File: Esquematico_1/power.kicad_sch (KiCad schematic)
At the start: 23 parts, among them IC1 AP2112K-3.3TRG1, U6 TPS54302DDCR

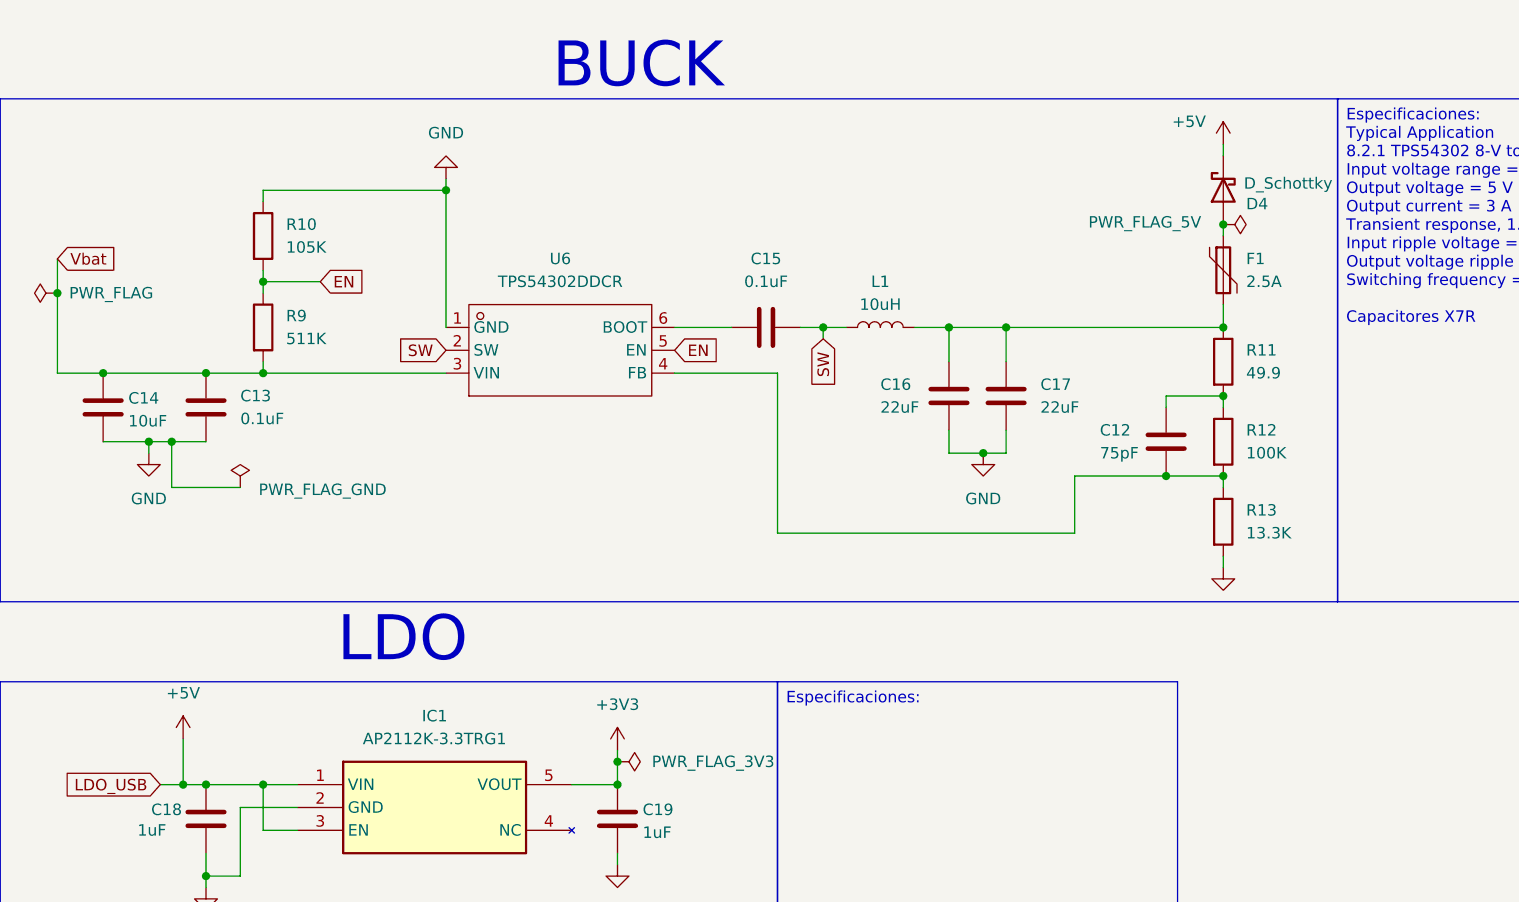
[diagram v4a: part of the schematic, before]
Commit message: Cambios netclasses, rules en el PCB, conección de los cristales
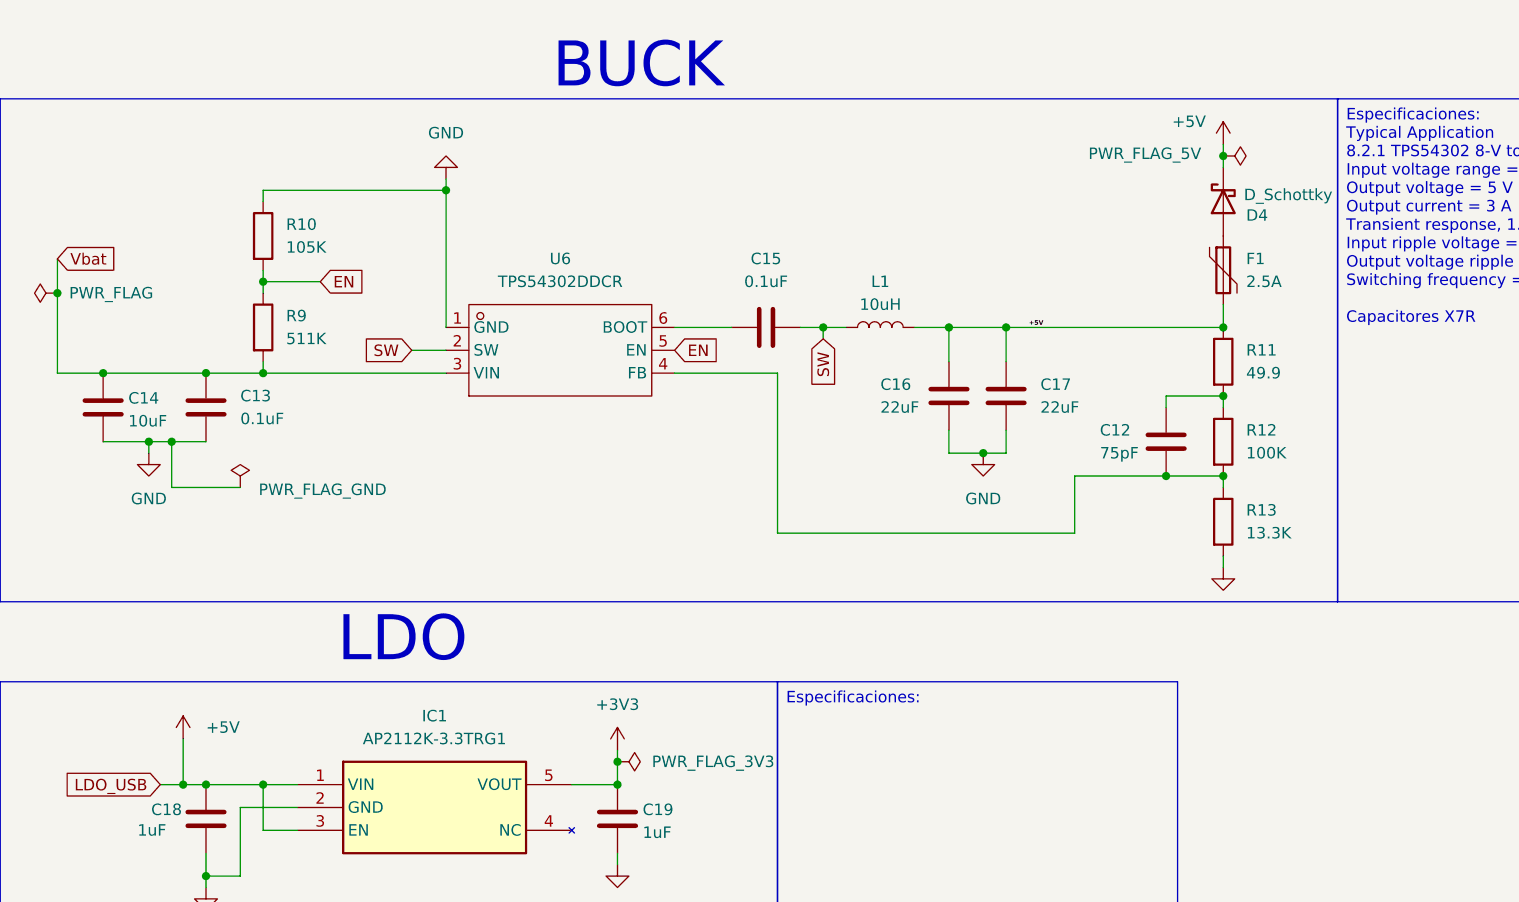
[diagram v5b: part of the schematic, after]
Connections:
- net +5V: now also C16.2, C17.2, F1.2, L1.2, R11.1
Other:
- moved on the sheet: D4
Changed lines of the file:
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@@
 	)
 	(junction
-		(at 158.75 35.56)
-		(diameter 0)
-		(color 0 0 0 0)
-	)
-	(junction
 		(at 52.07 52.07)
 		(diameter 0)
@@
 	)
 	(junction
+		(at 158.75 27.94)
+		(diameter 0)
+		(color 0 0 0 0)
+	)
+	(junction
 		(at 52.07 41.91)
 		(diameter 0)
@@
 	(wire
 		(pts
-			(xy 158.75 35.56) (xy 158.75 36.83)
-		)
-		(stroke
-			(width 0)
-			(type default)
-		)
-	)
-	(wire
-		(pts
 			(xy 114.3 46.99) (xy 111.76 46.99)
 		)
@@
 	(wire
 		(pts
+			(xy 68.58 49.53) (xy 72.39 49.53)
+		)
+		(stroke
+			(width 0)
+			(type default)
+		)
+	)
+	(wire
+		(pts
 			(xy 134.62 46.99) (xy 158.75 46.99)
 		)
@@
 	(wire
 		(pts
+			(xy 158.75 27.94) (xy 158.75 29.21)
+		)
+		(stroke
+			(width 0)
+			(type default)
+		)
+	)
+	(wire
+		(pts
 			(xy 49.53 100.33) (xy 49.53 107.95)
 		)
@@
 		)
 	)
+	(label "+5V"
+		(at 137.16 46.99 0)
+		(effects
+			(font
+				(size 0.508 0.508)
+				(thickness 0.254)
+				(bold yes)
+			)
+			(justify left bottom)
+		)
+	)
 	(global_label "Vbat"
 		(shape input)
@@
 	(global_label "SW"
 		(shape input)
-		(at 72.39 49.53 180)
+		(at 68.58 49.53 180)
 		(fields_autoplaced yes)
 		(effects
@@
 		)
 		(property "Intersheetrefs" "${INTERSHEET_REFS}"
-			(at 66.7439 49.53 0)
+			(at 62.9339 49.53 0)
 			(effects
 				(font
@@
 	(symbol
 		(lib_id "Device:D_Schottky")
-		(at 158.75 31.75 90)
+		(at 158.75 33.02 90)
 		(mirror x)
 		(unit 1)
@@
 		(dnp no)
 		(property "Reference" "D4"
-			(at 161.29 33.274 90)
+			(at 161.29 34.544 90)
 			(effects
 				(font
@@
 		)
 		(property "Value" "D_Schottky"
-			(at 161.036 30.988 90)
+			(at 161.036 32.258 90)
 			(effects
 				(font
@@
 		)
 		(property "Footprint" "Package_TO_SOT_SMD:SOT-23"
-			(at 158.75 31.75 0)
+			(at 158.75 33.02 0)
 			(effects
 				(font
@@
 		)
 		(property "Datasheet" "~"
-			(at 158.75 31.75 0)
+			(at 158.75 33.02 0)
 			(effects
 				(font
@@
 		)
 		(property "Description" "Schottky diode"
-			(at 158.75 31.75 0)
+			(at 158.75 33.02 0)
 			(effects
 				(font
@@
 	(symbol
 		(lib_id "power:PWR_FLAG")
-		(at 158.75 35.56 270)
+		(at 158.75 27.94 270)
 		(unit 1)
 		(exclude_from_sim no)
@@
 		(dnp no)
 		(property "Reference" "#FLG03"
-			(at 160.655 35.56 0)
+			(at 160.655 27.94 0)
 			(effects
 				(font
@@
 		)
 		(property "Value" "PWR_FLAG_5V"
-			(at 143.764 35.306 90)
+			(at 143.764 27.686 90)
 			(effects
 				(font
@@
 		)
 		(property "Footprint" ""
-			(at 158.75 35.56 0)
+			(at 158.75 27.94 0)
 			(effects
 				(font
@@
 		)
 		(property "Datasheet" "~"
-			(at 158.75 35.56 0)
+			(at 158.75 27.94 0)
 			(effects
 				(font
@@
 		)
 		(property "Description" "Special symbol for telling ERC where power comes from"
-			(at 158.75 35.56 0)
+			(at 158.75 27.94 0)
 			(effects
 				(font
@@
 		)
 		(instances
-			(project ""
+			(project "Esquematico_1"
 				(path "/de2d80c1-c21c-478d-b724-17659b714c38/46661298-47a8-4fc3-89be-a6732b8d105c"
 					(reference "#FLG03")
@@
 		)
 		(property "Value" "+5V"
-			(at 43.18 87.63 0)
+			(at 45.72 91.4399 0)
 			(effects
 				(font
 					(size 1.27 1.27)
 				)
+				(justify left)
 			)
 		)

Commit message: Diodo de mierda
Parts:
- D2: footprint Diode_SMD:D_SOD-523 -> Diode_SMD:D_SMB_Handsoldering
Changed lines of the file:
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@@
 			)
 		)
-		(property "Footprint" "Diode_SMD:D_SOD-523"
+		(property "Footprint" "Diode_SMD:D_SMB_Handsoldering"
 			(at 60.325 162.56 0)
 			(effects

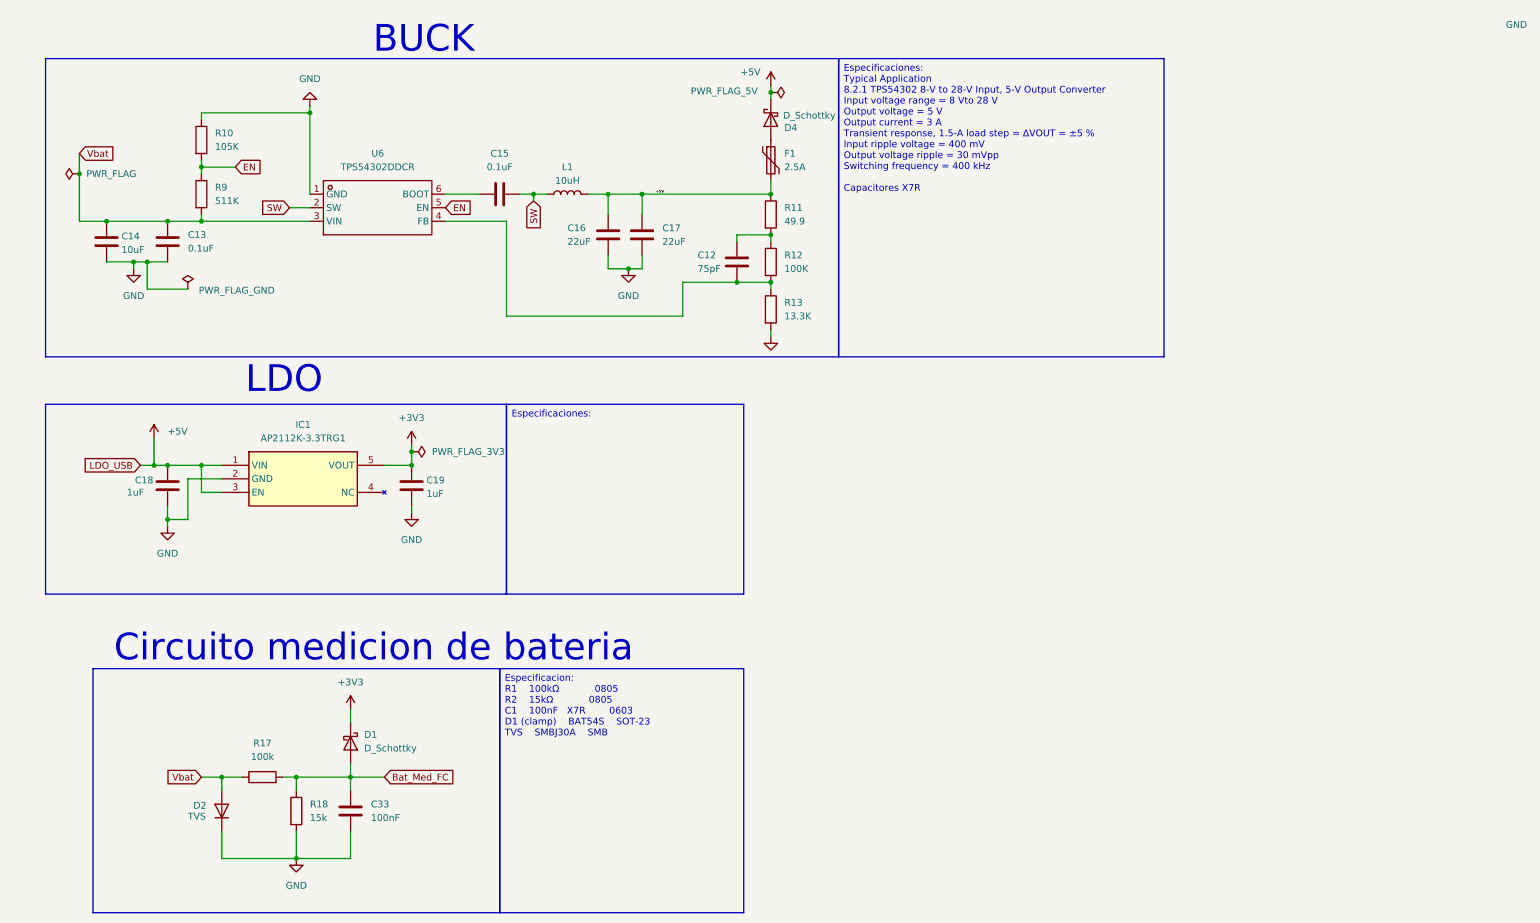
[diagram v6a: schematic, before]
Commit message: Update PCB backlayer
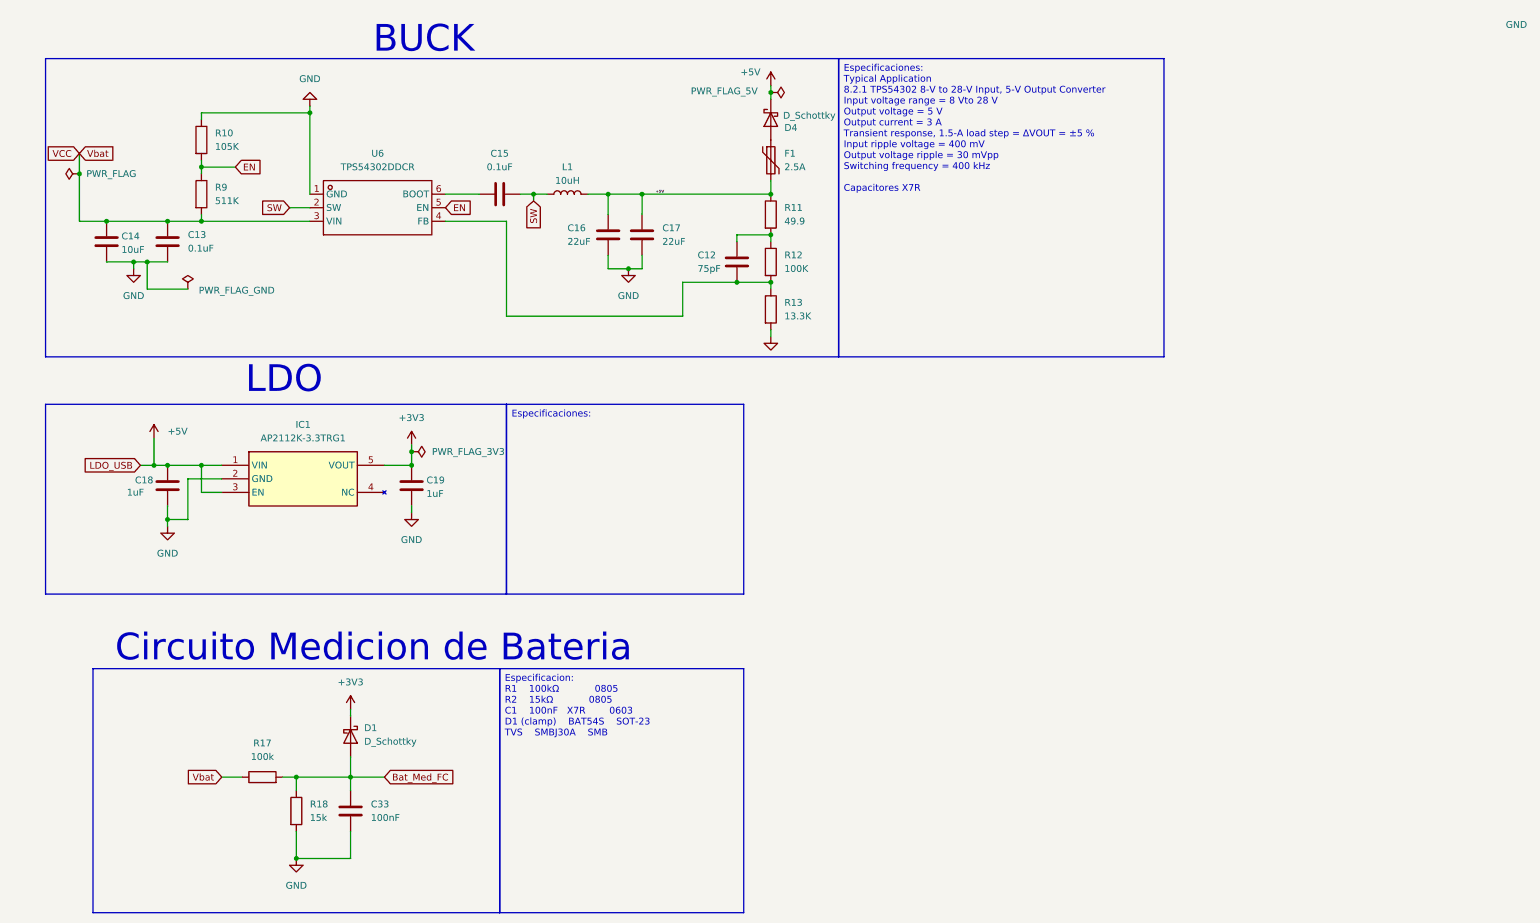
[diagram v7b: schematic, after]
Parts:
- removed D2: TVS, Diode_SMD:D_SMB_Handsoldering, symbol Diode:1N4148WT
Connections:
- net Vbat renamed VCC
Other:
- note added: "Circuito Medicion de Bateria"
- note removed: "Circuito medicion de bateria"
- moved on the sheet: D1
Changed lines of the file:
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@@
 		)
 	)
-	(text "Circuito medicion de bateria\n"
+	(text "Circuito Medicion de Bateria\n"
 		(exclude_from_sim no)
 		(at 84.328 132.08 0)
@@
 	)
 	(junction
-		(at 55.88 156.21)
-		(diameter 0)
-		(color 0 0 0 0)
-	)
-	(junction
 		(at 158.75 46.99)
 		(diameter 0)
@@
 	(wire
 		(pts
-			(xy 80.01 143.51) (xy 80.01 146.05)
+			(xy 80.01 143.51) (xy 80.01 144.78)
 		)
 		(stroke
@@
 	(wire
 		(pts
-			(xy 80.01 153.67) (xy 80.01 156.21)
+			(xy 80.01 152.4) (xy 80.01 156.21)
 		)
 		(stroke
@@
 	(wire
 		(pts
-			(xy 52.07 156.21) (xy 55.88 156.21)
+			(xy 55.88 156.21) (xy 59.69 156.21)
 		)
 		(stroke
@@
 	(wire
 		(pts
-			(xy 55.88 156.21) (xy 59.69 156.21)
-		)
-		(stroke
-			(width 0)
-			(type default)
-		)
-	)
-	(wire
-		(pts
 			(xy 72.39 31.75) (xy 72.39 46.99)
 		)
@@
 	(wire
 		(pts
-			(xy 55.88 171.45) (xy 69.85 171.45)
-		)
-		(stroke
-			(width 0)
-			(type default)
-		)
-	)
-	(wire
-		(pts
-			(xy 55.88 156.21) (xy 55.88 158.75)
-		)
-		(stroke
-			(width 0)
-			(type default)
-		)
-	)
-	(wire
-		(pts
 			(xy 29.21 43.18) (xy 29.21 52.07)
 		)
@@
 	(wire
 		(pts
-			(xy 55.88 166.37) (xy 55.88 171.45)
-		)
-		(stroke
-			(width 0)
-			(type default)
-		)
-	)
-	(wire
-		(pts
 			(xy 43.18 92.71) (xy 43.18 97.79)
 		)
@@
 		)
 	)
+	(global_label "VCC"
+		(shape input)
+		(at 29.21 39.37 180)
+		(fields_autoplaced yes)
+		(effects
+			(font
+				(size 1.27 1.27)
+			)
+			(justify right)
+		)
+		(property "Intersheetrefs" "${INTERSHEET_REFS}"
+			(at 22.5962 39.37 0)
+			(effects
+				(font
+					(size 1.27 1.27)
+				)
+				(justify right)
+				(hide yes)
+			)
+		)
+	)
 	(global_label "LDO_USB"
 		(shape input)
@@
 	(global_label "Vbat"
 		(shape input)
-		(at 52.07 156.21 180)
+		(at 55.88 156.21 180)
 		(fields_autoplaced yes)
 		(effects
@@
 		)
 		(property "Intersheetrefs" "${INTERSHEET_REFS}"
-			(at 44.9725 156.21 0)
+			(at 48.7825 156.21 0)
 			(effects
 				(font
@@
 	)
 	(symbol
-		(lib_id "Diode:1N4148WT")
-		(at 55.88 162.56 90)
-		(unit 1)
-		(exclude_from_sim no)
-		(in_bom yes)
-		(on_board yes)
-		(dnp no)
-		(property "Reference" "D2"
-			(at 50.546 161.544 90)
-			(effects
-				(font
-					(size 1.27 1.27)
-				)
-				(justify right)
-			)
-		)
-		(property "Value" "TVS"
-			(at 49.53 163.576 90)
-			(effects
-				(font
-					(size 1.27 1.27)
-				)
-				(justify right)
-			)
-		)
-		(property "Footprint" "Diode_SMD:D_SMB_Handsoldering"
-			(at 60.325 162.56 0)
-			(effects
-				(font
-					(size 1.27 1.27)
-				)
-				(hide yes)
-			)
-		)
-		(property "Datasheet" "https://www.diodes.com/assets/Datasheets/ds30396.pdf"
-			(at 55.88 162.56 0)
-			(effects
-				(font
-					(size 1.27 1.27)
-				)
-				(hide yes)
-			)
-		)
-		(property "Description" "75V 0.15A Fast switching Diode, SOD-523"
-			(at 55.88 162.56 0)
-			(effects
-				(font
-					(size 1.27 1.27)
-				)
-				(hide yes)
-			)
-		)
-		(property "Sim.Device" "D"
-			(at 55.88 162.56 0)
-			(effects
-				(font
-					(size 1.27 1.27)
-				)
-				(hide yes)
-			)
-		)
-		(property "Sim.Pins" "1=K 2=A"
-			(at 55.88 162.56 0)
-			(effects
-				(font
-					(size 1.27 1.27)
-				)
-				(hide yes)
-			)
-		)
-		(pin "2"
-		)
-		(pin "1"
-		)
-		(instances
-			(project "power"
-				(path "/14e83f21-a583-4056-88d1-a5aa5c330b39"
-					(reference "D1")
-					(unit 1)
-				)
-			)
-			(project ""
-				(path "/de2d80c1-c21c-478d-b724-17659b714c38/46661298-47a8-4fc3-89be-a6732b8d105c"
-					(reference "D2")
-					(unit 1)
-				)
-			)
-		)
-	)
-	(symbol
 		(lib_id "TPS54302DDCR:TPS54302DDCR_C311983")
 		(at 85.09 49.53 0)
@@
 	(symbol
 		(lib_id "Device:D_Schottky")
-		(at 80.01 149.86 270)
+		(at 80.01 148.59 270)
 		(unit 1)
 		(exclude_from_sim no)
@@
 		(fields_autoplaced yes)
 		(property "Reference" "D1"
-			(at 82.55 148.2724 90)
+			(at 82.55 147.0024 90)
 			(effects
 				(font
@@
 		)
 		(property "Value" "D_Schottky"
-			(at 82.55 150.8124 90)
+			(at 82.55 149.5424 90)
 			(effects
 				(font
@@
 		)
 		(property "Footprint" "Package_TO_SOT_SMD:SOT-23"
-			(at 80.01 149.86 0)
+			(at 80.01 148.59 0)
 			(effects
 				(font
@@
 		)
 		(property "Datasheet" "~"
-			(at 80.01 149.86 0)
+			(at 80.01 148.59 0)
 			(effects
 				(font
@@
 		)
 		(property "Description" "Schottky diode"
-			(at 80.01 149.86 0)
+			(at 80.01 148.59 0)
 			(effects
 				(font

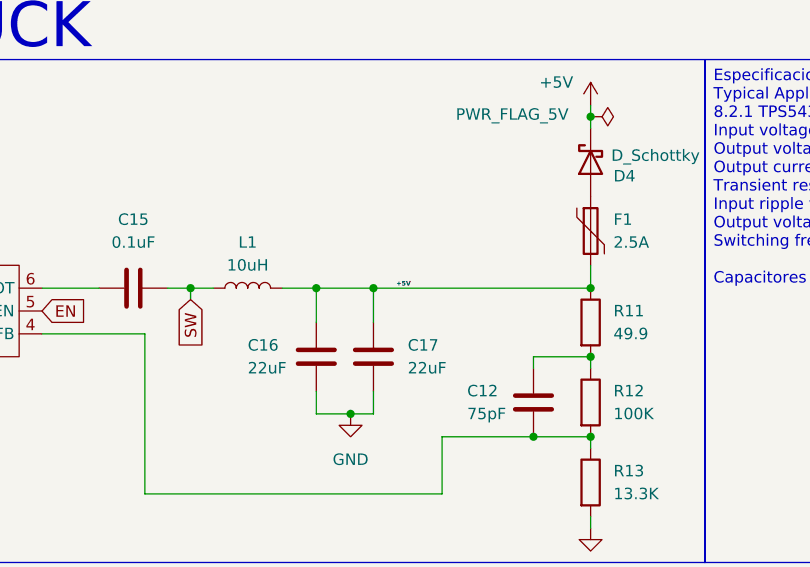
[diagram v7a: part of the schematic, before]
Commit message: Update buck y LDO
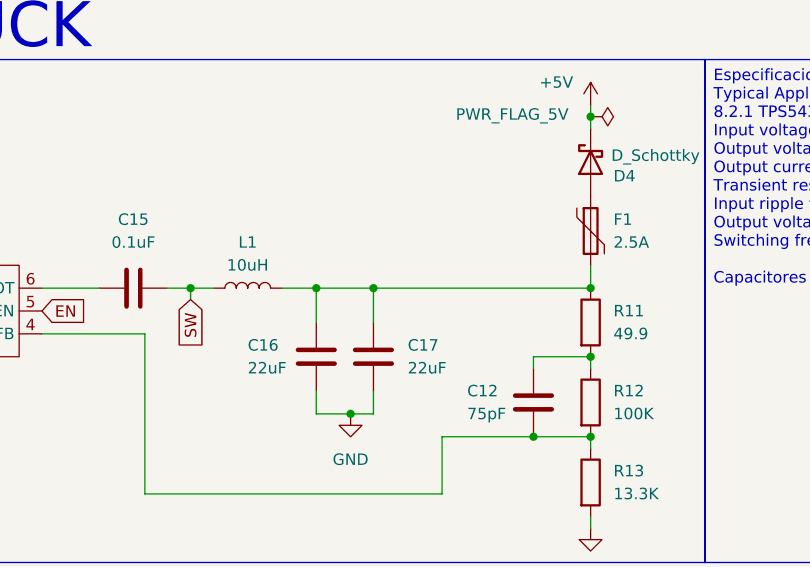
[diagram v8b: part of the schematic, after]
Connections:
- net +5V: no longer C16.2, C17.2, F1.2, L1.2, R11.1
- new net: C16.2, C17.2, F1.2, L1.2, R11.1
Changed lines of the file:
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@@
-		)
-	)
-	(label "+5V"
-		(at 137.16 46.99 0)
-		(effects
-			(font
-				(size 0.508 0.508)
-				(thickness 0.254)
-				(bold yes)
-			)
-			(justify left bottom)
 		)
 	)
